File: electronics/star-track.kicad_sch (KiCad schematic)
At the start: 22 parts, among them J1 XT60 female, J2 Hand unit, 8 pins, J3 Joystick module, J4 AZ motor, J5 ALT motor, SW2 E-stop (NC), SW3 Push button, SW4 Push button, SW5 Push button, U1 DC-DC 5V module, U2 GY-GPS6MV2

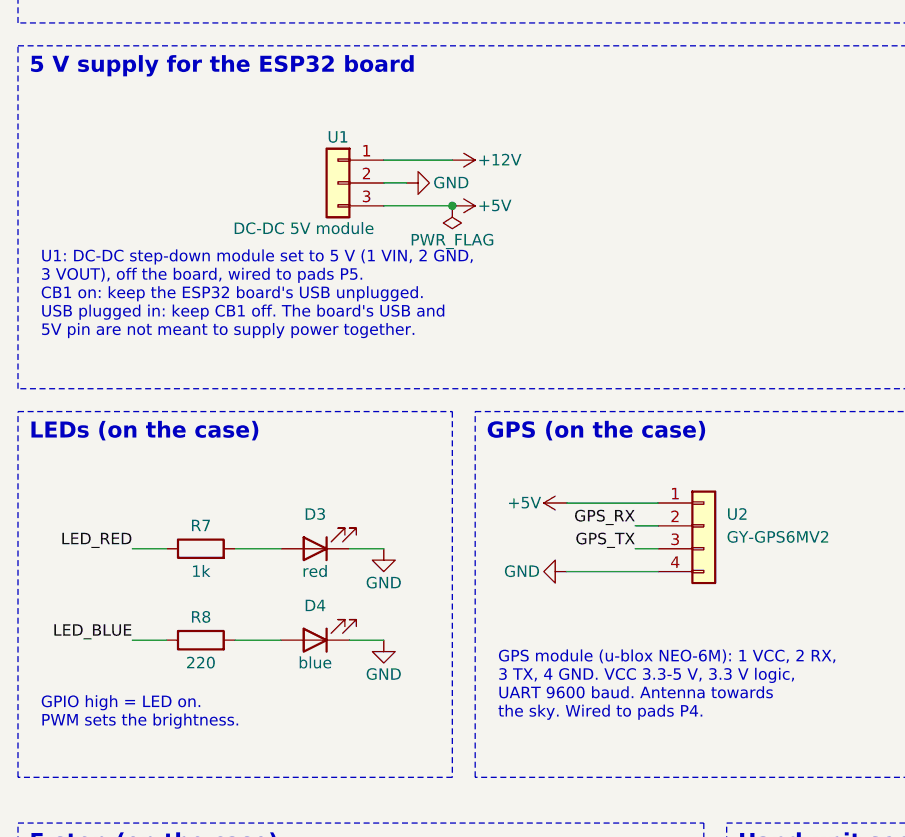
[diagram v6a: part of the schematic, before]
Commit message: Add a Schottky diode on the 5 V supply, use SMD resistors, re-route the PCB
- D5 (PMEG3005EB) between the DC-DC output and the ESP32 board's 5V pin, so
  USB and the 12 V supply can be connected at the same time.
- R3, R7, R8 as 0603 and D5 as SOD-523, for hand soldering; R8 now 330 ohm.
- PCB: C6 moved next to the azimuth driver's VM pin, new placement and
  routing, antenna keep-out with no copper, orientation labels on the driver
  sockets and the ESP32 board, silkscreen strokes of at least 0.15 mm.
- Gerbers, renders and docs updated.

Co-Authored-By: Claude Opus 5.5 <noreply@anthropic.com>
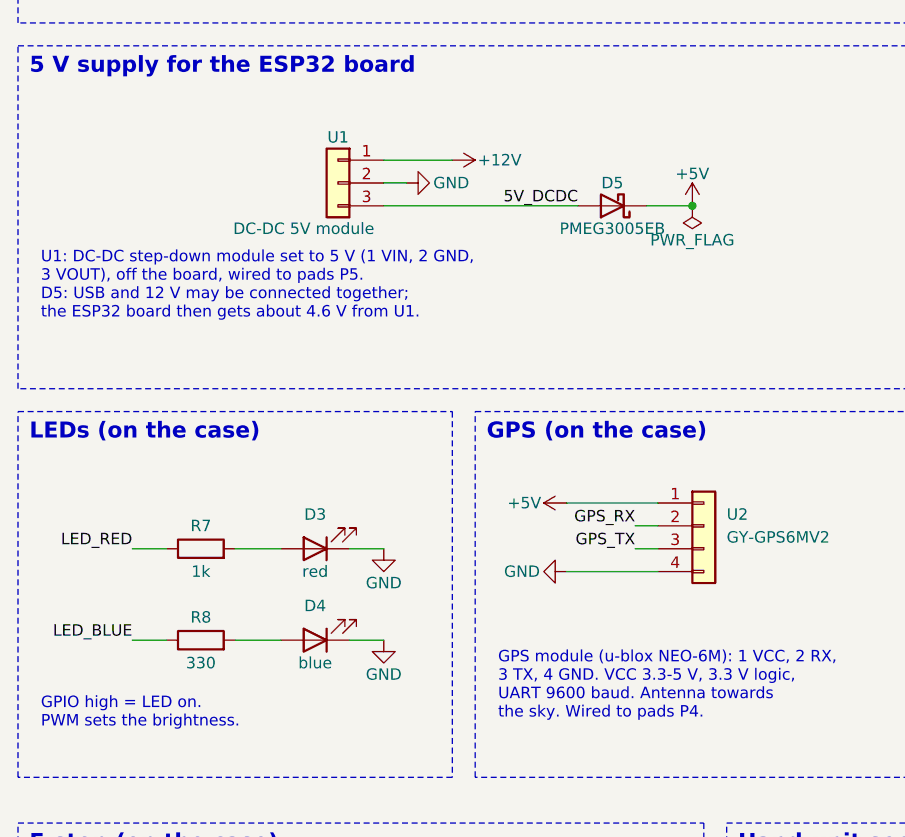
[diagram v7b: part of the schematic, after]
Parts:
- removed D3: red, symbol Device:LED
- removed D4: blue, symbol Device:LED
- removed J4: AZ motor, Connector_PinHeader_2.54mm:PinHeader_1x04_P2.54mm_Vertical, symbol Connector_Generic:Conn_01x04
- removed J5: ALT motor, Connector_PinHeader_2.54mm:PinHeader_1x04_P2.54mm_Vertical, symbol Connector_Generic:Conn_01x04
- removed R3: 10k, Resistor_THT:R_Axial_DIN0207_L6.3mm_D2.5mm_P7.62mm_Horizontal, symbol Device:R
- removed SW3: Push button, symbol Switch:SW_Push
- added A3: TMC2209 ALT, star-track:TMC2209_StepStick_Socket, symbol star-track:TMC2209_module
- added D5: PMEG3005EB, Diode_SMD:D_SOD-523, symbol Device:D_Schottky
- added J2: Hand unit, 8 pins, symbol Connector_Generic:Conn_01x08
- added R8: 330, Resistor_SMD:R_0603_1608Metric_Pad0.98x0.95mm_HandSolder, symbol Device:R
- added SW2: E-stop (NC), symbol Switch:SW_Push_Open
- added SW5: Push button, symbol Switch:SW_Push
- added U2: GY-GPS6MV2, symbol Connector_Generic:Conn_01x04
- D3: renamed from R8; value 220 -> red; footprint Resistor_THT:R_Axial_DIN0207_L6.3mm_D2.5mm_P10.16mm_Horizontal -> (none); symbol Device:R -> Device:LED
- D4: renamed from U2; value GY-GPS6MV2 -> blue; symbol Connector_Generic:Conn_01x04 -> Device:LED
- J4: renamed from A3; value TMC2209 ALT -> AZ motor; footprint star-track:TMC2209_StepStick_Socket -> Connector_PinHeader_2.54mm:PinHeader_1x04_P2.54mm_Vertical; symbol star-track:TMC2209_module -> Connector_Generic:Conn_01x04
- J5: renamed from SW2; value E-stop (NC) -> ALT motor; footprint (none) -> Connector_PinHeader_2.54mm:PinHeader_1x04_P2.54mm_Vertical; symbol Switch:SW_Push_Open -> Connector_Generic:Conn_01x04
- R3: renamed from J2; value Hand unit, 8 pins -> 10k; footprint (none) -> Resistor_SMD:R_0603_1608Metric_Pad0.98x0.95mm_HandSolder; symbol Connector_Generic:Conn_01x08 -> Device:R
- R7: footprint Resistor_THT:R_Axial_DIN0207_L6.3mm_D2.5mm_P10.16mm_Horizontal -> Resistor_SMD:R_0603_1608Metric_Pad0.98x0.95mm_HandSolder
- renumbered SW4 to SW3, SW5 to SW4
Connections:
- net +12V: now also A3.9 (VM); no longer J4.9 (VM)
- net +3V3: now also R3.1, A3.15 (VIO), A3.3 (MS2), J2.2 (Pin_2); no longer J4.15 (VIO), J4.3 (MS2), R3.2 (Pin_2)
- net +5V: now also D5.1 (K), U2.1 (Pin_1); no longer D4.1 (Pin_1), U1.3 (Pin_3)
- net ALT_DIR: now also A3.8 (DIR); no longer J4.8 (DIR)
- net ALT_STEP: now also A3.7 (STEP); no longer J4.7 (STEP)
- net BTN1: now also SW3.1, J2.6 (Pin_6); no longer R3.6 (Pin_6)
- net BTN2: now also SW4.1, J2.7 (Pin_7); no longer R3.7 (Pin_7), SW3.1
- net BTN3: now also J2.8 (Pin_8), SW5.1; no longer R3.8 (Pin_8), SW4.1
- net DRV_EN: now also R3.2, A3.1 (EN), SW2.2 (B); no longer J4.1 (EN), J5.2 (B)
- net EN_OUT: now also SW2.1 (A); no longer J5.1 (A)
- net GND: now also D3.1 (K), D4.1 (K), A3.10 (GND), A3.16 (GND), A3.2 (MS1), J2.1 (Pin_1), SW5.2, U2.4 (Pin_4); no longer D4.4 (Pin_4), J4.10 (GND), J4.16 (GND), J4.2 (MS1), R3.1 (Pin_1)
- net GPS_RX: now also U2.2 (Pin_2); no longer D4.2 (Pin_2)
- net GPS_TX: now also U2.3 (Pin_3); no longer D4.3 (Pin_3)
- net JOY_SW: now also J2.5 (Pin_5); no longer R3.5 (Pin_5)
- net JOY_X: now also J2.3 (Pin_3); no longer R3.3 (Pin_3)
- net JOY_Y: now also J2.4 (Pin_4); no longer R3.4 (Pin_4)
- net LED_BLUE: now also R8.1; no longer D3.1
- net at R7.2: now also D3.2 (A)
- net at J4.4 (Pin_4): now also A2.11 (2B)
- net at A2.14 (1B): now also J4.1 (Pin_1)
- net at A2.13 (1A): now also J4.2 (Pin_2)
- net at A2.12 (2A): now also J4.3 (Pin_3)
- new net: A3.11 (2B), J5.4 (Pin_4)
- new net: A3.12 (2A), J5.3 (Pin_3)
- new net: A3.13 (1A), J5.2 (Pin_2)
- new net: A3.14 (1B), J5.1 (Pin_1)
- new net: D4.2 (A), R8.2
- new net 5V_DCDC: D5.2 (A), U1.3 (Pin_3)
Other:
- note added: "U1: DC-DC step-down module set to 5 V (1 VIN, 2 GND, 3 VOUT), off the board, wired to pads P5. D5: USB and 12 V may be connected together; the ESP32 board then gets about 4.6 V from U1."
- note removed: "U1: DC-DC step-down module set to 5 V (1 VIN, 2 GND, 3 VOUT), off the board, wired to pads P5. CB1 on: keep the ESP32 board's USB unplugged. USB plugged in: keep CB1 off. The board's USB and 5V pin are not meant to supply power together."
- moved on the sheet: SW3, SW4
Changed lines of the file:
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@@
   (junction (at 43.18 38.1) (diameter 0) (color 0 0 0 0))
   (junction (at 53.34 172.72) (diameter 0) (color 0 0 0 0))
-  (junction (at 68.58 83.82) (diameter 0) (color 0 0 0 0))
   (junction (at 76.2 33.02) (diameter 0) (color 0 0 0 0))
+  (junction (at 95.25 83.82) (diameter 0) (color 0 0 0 0))
   (junction (at 175.26 48.26) (diameter 0) (color 0 0 0 0))
   (junction (at 190.5 111.76) (diameter 0) (color 0 0 0 0))
@@
   (wire (pts (xy 60.96 78.74) (xy 68.58 78.74)) (stroke (width 0) (type default)))
   (wire (pts (xy 60.96 81.28) (xy 63.5 81.28)) (stroke (width 0) (type default)))
-  (wire (pts (xy 60.96 83.82) (xy 68.58 83.82)) (stroke (width 0) (type default)))
+  (wire (pts (xy 60.96 83.82) (xy 82.55 83.82)) (stroke (width 0) (type default)))
+  (wire (pts (xy 90.17 83.82) (xy 95.25 83.82)) (stroke (width 0) (type default)))
   (wire (pts (xy 33.02 121.92) (xy 36.83 121.92)) (stroke (width 0) (type default)))
   (wire (pts (xy 44.45 121.92) (xy 49.53 121.92)) (stroke (width 0) (type default)))
@@
   (rectangle (start 167.64 152.4) (end 297.18 205.74) (stroke (width 0) (type dash)) (fill (type none)))
   (rectangle (start 299.72 152.4) (end 406.4 205.74) (stroke (width 0) (type dash)) (fill (type none)))
+  (label "5V_DCDC" (at 82.55 83.82 180) (fields_autoplaced) (effects (font (size 1.27 1.27)) (justify right bottom)))
   (label "LED_RED" (at 33.02 121.92 180) (fields_autoplaced) (effects (font (size 1.27 1.27)) (justify right bottom)))
   (label "LED_BLUE" (at 33.02 132.08 180) (fields_autoplaced) (effects (font (size 1.27 1.27)) (justify right bottom)))
@@
   (text "J1: female XT60 on the case, for the battery\n(LiFePO4 12.8 V 6 Ah with BMS) or a lab supply\n(12-14 V, current limit about 2 A).\nThe battery is charged off the mount.\nCB1: resettable breaker switch, 3-5 A, rated for DC." (at 22.86 46.99 0) (effects (font (size 1.27 1.27)) (justify left top)))
   (text "5 V supply for the ESP32 board" (at 21.59 67.31 0) (effects (font (size 1.778 1.778) bold) (justify left top)))
-  (text "U1: DC-DC step-down module set to 5 V (1 VIN, 2 GND,\n3 VOUT), off the board, wired to pads P5.\nCB1 on: keep the ESP32 board's USB unplugged.\nUSB plugged in: keep CB1 off. The board's USB and\n5V pin are not meant to supply power together." (at 22.86 88.9 0) (effects (font (size 1.27 1.27)) (justify left top)))
+  (text "U1: DC-DC step-down module set to 5 V (1 VIN, 2 GND,\n3 VOUT), off the board, wired to pads P5.\nD5: USB and 12 V may be connected together;\nthe ESP32 board then gets about 4.6 V from U1." (at 22.86 88.9 0) (effects (font (size 1.27 1.27)) (justify left top)))
   (text "LEDs (on the case)" (at 21.59 107.95 0) (effects (font (size 1.778 1.778) bold) (justify left top)))
   (text "GPIO high = LED on.\nPWM sets the brightness." (at 22.86 138.43 0) (effects (font (size 1.27 1.27)) (justify left top)))
@@
     )
   )
-  (symbol (lib_id "power:+5V") (at 68.58 83.82 270) (unit 1)
-    (in_bom no) (on_board no) (dnp no)
-    (property "Reference" "#PWR07" (at 68.58 83.82 90) (effects (font (size 1.27 1.27)) hide))
-    (property "Value" "+5V" (at 73.286 83.82 90) (effects (font (size 1.27 1.27))))
-    (property "Footprint" "" (at 68.58 83.82 90) (effects (font (size 1.27 1.27)) hide))
-    (property "Datasheet" "~" (at 68.58 83.82 90) (effects (font (size 1.27 1.27)) hide))
+  (symbol (lib_id "Device:D_Schottky") (at 86.36 83.82 180) (unit 1)
+    (in_bom yes) (on_board yes) (dnp no)
+    (property "Reference" "D5" (at 86.36 81.28 0) (effects (font (size 1.27 1.27))))
+    (property "Value" "PMEG3005EB" (at 86.36 86.36 0) (effects (font (size 1.27 1.27))))
+    (property "Footprint" "Diode_SMD:D_SOD-523" (at 86.36 83.82 0) (effects (font (size 1.27 1.27)) hide))
+    (property "Datasheet" "~" (at 86.36 83.82 0) (effects (font (size 1.27 1.27)) hide))
+    (pin "1")
+    (pin "2")
+    (instances
+      (project "star-track"
+        (path "/1c6c1e4f-2454-572f-9ff8-455722d04c0d" (reference "D5") (unit 1))
+      )
+    )
+  )
+  (symbol (lib_id "power:+5V") (at 95.25 83.82 0) (unit 1)
+    (in_bom no) (on_board no) (dnp no)
+    (property "Reference" "#PWR07" (at 95.25 83.82 0) (effects (font (size 1.27 1.27)) hide))
+    (property "Value" "+5V" (at 95.25 80.264 0) (effects (font (size 1.27 1.27))))
+    (property "Footprint" "" (at 95.25 83.82 0) (effects (font (size 1.27 1.27)) hide))
+    (property "Datasheet" "~" (at 95.25 83.82 0) (effects (font (size 1.27 1.27)) hide))
     (pin "1")
     (instances
@@
     )
   )
-  (symbol (lib_id "power:PWR_FLAG") (at 68.58 83.82 180) (unit 1)
-    (in_bom no) (on_board no) (dnp no)
-    (property "Reference" "#FLG08" (at 68.58 83.82 0) (effects (font (size 1.27 1.27)) hide))
-    (property "Value" "PWR_FLAG" (at 68.58 87.63 0) (effects (font (size 1.27 1.27))))
-    (property "Footprint" "" (at 68.58 83.82 0) (effects (font (size 1.27 1.27)) hide))
-    (property "Datasheet" "~" (at 68.58 83.82 0) (effects (font (size 1.27 1.27)) hide))
+  (symbol (lib_id "power:PWR_FLAG") (at 95.25 83.82 180) (unit 1)
+    (in_bom no) (on_board no) (dnp no)
+    (property "Reference" "#FLG08" (at 95.25 83.82 0) (effects (font (size 1.27 1.27)) hide))
+    (property "Value" "PWR_FLAG" (at 95.25 87.63 0) (effects (font (size 1.27 1.27))))
+    (property "Footprint" "" (at 95.25 83.82 0) (effects (font (size 1.27 1.27)) hide))
+    (property "Datasheet" "~" (at 95.25 83.82 0) (effects (font (size 1.27 1.27)) hide))
     (pin "1")
     (instances
@@
     (property "Reference" "R7" (at 40.64 119.38 90) (effects (font (size 1.27 1.27))))
     (property "Value" "1k" (at 40.64 124.46 90) (effects (font (size 1.27 1.27))))
-    (property "Footprint" "Resistor_THT:R_Axial_DIN0207_L6.3mm_D2.5mm_P10.16mm_Horizontal" (at 40.64 121.92 90) (effects (font (size 1.27 1.27)) hide))
+    (property "Footprint" "Resistor_SMD:R_0603_1608Metric_Pad0.98x0.95mm_HandSolder" (at 40.64 121.92 90) (effects (font (size 1.27 1.27)) hide))
     (property "Datasheet" "~" (at 40.64 121.92 90) (effects (font (size 1.27 1.27)) hide))
     (pin "1")
@@
     (in_bom yes) (on_board yes) (dnp no)
     (property "Reference" "R8" (at 40.64 129.54 90) (effects (font (size 1.27 1.27))))
-    (property "Value" "220" (at 40.64 134.62 90) (effects (font (size 1.27 1.27))))
-    (property "Footprint" "Resistor_THT:R_Axial_DIN0207_L6.3mm_D2.5mm_P10.16mm_Horizontal" (at 40.64 132.08 90) (effects (font (size 1.27 1.27)) hide))
+    (property "Value" "330" (at 40.64 134.62 90) (effects (font (size 1.27 1.27))))
+    (property "Footprint" "Resistor_SMD:R_0603_1608Metric_Pad0.98x0.95mm_HandSolder" (at 40.64 132.08 90) (effects (font (size 1.27 1.27)) hide))
     (property "Datasheet" "~" (at 40.64 132.08 90) (effects (font (size 1.27 1.27)) hide))
     (pin "1")
@@
     (property "Reference" "R3" (at 55.88 167.64 0) (effects (font (size 1.27 1.27)) (justify left)))
     (property "Value" "10k" (at 55.88 170.18 0) (effects (font (size 1.27 1.27)) (justify left)))
-    (property "Footprint" "Resistor_THT:R_Axial_DIN0207_L6.3mm_D2.5mm_P7.62mm_Horizontal" (at 53.34 168.91 0) (effects (font (size 1.27 1.27)) hide))
+    (property "Footprint" "Resistor_SMD:R_0603_1608Metric_Pad0.98x0.95mm_HandSolder" (at 53.34 168.91 0) (effects (font (size 1.27 1.27)) hide))
     (property "Datasheet" "~" (at 53.34 168.91 0) (effects (font (size 1.27 1.27)) hide))
     (pin "1")
